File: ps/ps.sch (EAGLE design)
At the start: 73 parts, among them IC1 LM675, J1 NE-2, Q1 NPN-D, Q2 NPN-D, U2 LM317, U3 TLC555CD, U4 LM317, U5 LM317

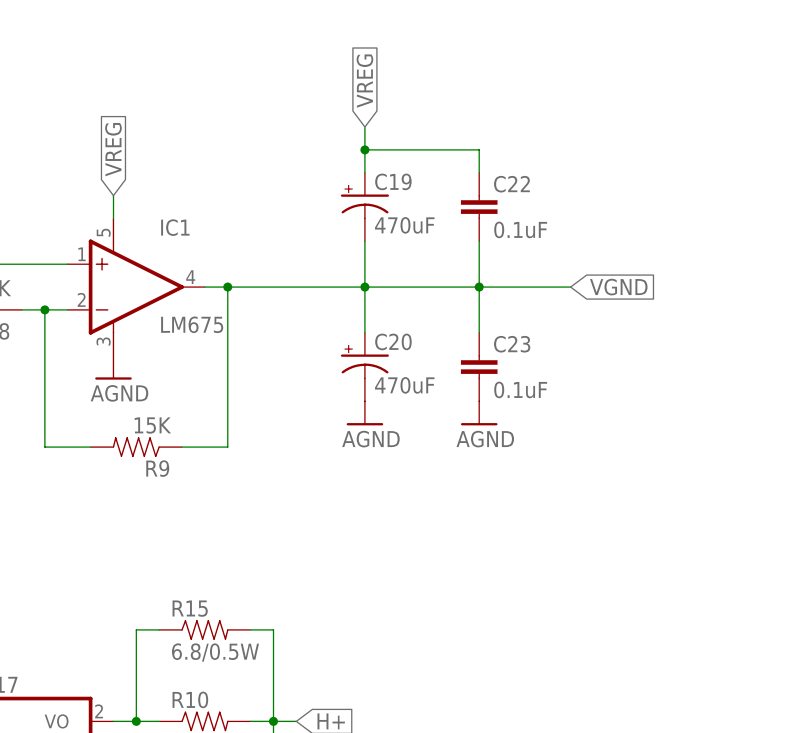
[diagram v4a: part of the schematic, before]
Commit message: Unneeded caps removed
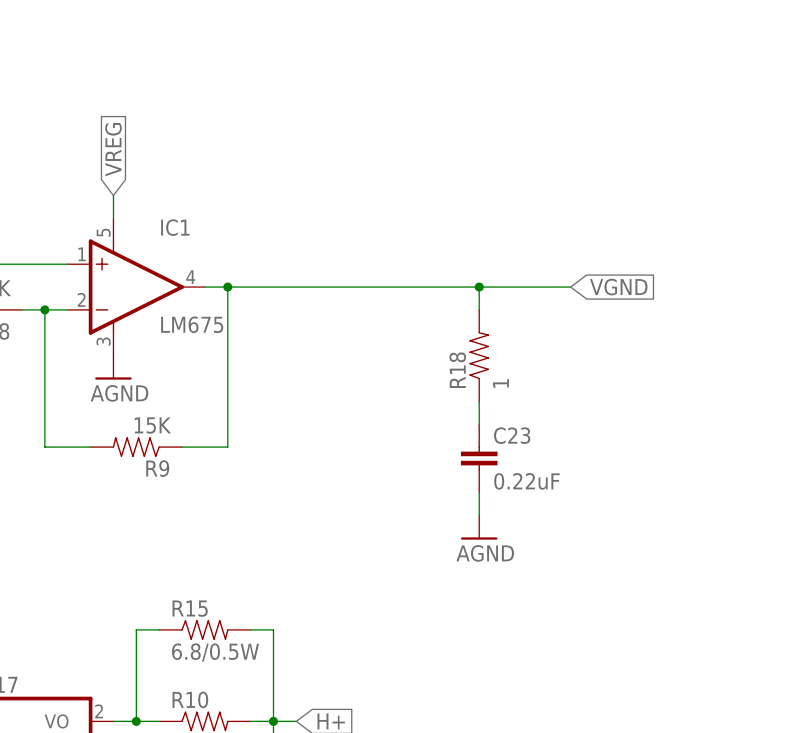
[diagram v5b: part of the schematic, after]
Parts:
- removed C19, C20: 470uF, SparkFun-Capacitors:CAP_POLPTH4
- removed C22: 0.1uF, SparkFun-Capacitors:0.1UF-25V-5%(0603)
- added R18: 1, SparkFun-Resistors:RESISTORPTH-1/4W
- C23: value 0.1uF -> 0.22uF; device SparkFun-Capacitors:0.1UF-25V-5%(0603) -> SparkFun-Capacitors:0.22UF-25V-10%(0603)
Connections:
- new net N$17: C23.1, R18.1
- net AGND: no longer C20.-
- net VGND: now also R18.2; no longer C19.-, C20.+, C22.2, C23.1
- net VREG: no longer C19.+, C22.1
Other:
- moved on the sheet: C23
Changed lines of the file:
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@@
 <part name="C2" library="SparkFun-Capacitors" deviceset="CAP_POL" device="PTH4" value="470uF"/>
 <part name="SUPPLY1" library="SparkFun-Aesthetics" deviceset="VCC" device=""/>
-<part name="C20" library="SparkFun-Capacitors" deviceset="CAP_POL" device="PTH4" value="470uF"/>
-<part name="C19" library="SparkFun-Capacitors" deviceset="CAP_POL" device="PTH4" value="470uF"/>
-<part name="C22" library="SparkFun-Capacitors" deviceset="0.1UF-25V-5%(0603)" device="" value="0.1uF"/>
-<part name="C23" library="SparkFun-Capacitors" deviceset="0.1UF-25V-5%(0603)" device="" value="0.1uF"/>
+<part name="C23" library="SparkFun-Capacitors" deviceset="0.22UF-25V-10%(0603)" device="" value="0.22uF"/>
 <part name="LOGO1" library="my" deviceset="LOGO-MANTIS" device=""/>
 <part name="X1" library="con-wago-508" deviceset="W237-02P" device=""/>
@@
 <part name="U$1" library="SparkFun-Aesthetics" deviceset="AGND" device=""/>
 <part name="U$2" library="SparkFun-Aesthetics" deviceset="AGND" device=""/>
-<part name="U$3" library="SparkFun-Aesthetics" deviceset="AGND" device=""/>
 <part name="U$4" library="SparkFun-Aesthetics" deviceset="AGND" device=""/>
 <part name="U$5" library="SparkFun-Aesthetics" deviceset="AGND" device=""/>
@@
 <part name="R16" library="SparkFun-Resistors" deviceset="RESISTOR" device="PTH-1/4W" value="0.33"/>
 <part name="R17" library="SparkFun-Resistors" deviceset="RESISTOR" device="PTH-1/4W-VERT" value="1"/>
+<part name="R18" library="SparkFun-Resistors" deviceset="RESISTOR" device="PTH-1/4W" value="1"/>
 </parts>
 <sheets>
@@
 <instance part="C2" gate="G$1" x="15.24" y="154.94"/>
 <instance part="SUPPLY1" gate="G$1" x="12.7" y="172.72" rot="R90"/>
-<instance part="C20" gate="G$1" x="266.7" y="200.66"/>
-<instance part="C19" gate="G$1" x="266.7" y="218.44"/>
-<instance part="C22" gate="G$1" x="279.4" y="215.9"/>
-<instance part="C23" gate="G$1" x="279.4" y="198.12"/>
+<instance part="C23" gate="G$1" x="279.4" y="187.96"/>
 <instance part="LOGO1" gate="G$1" x="175.26" y="43.18"/>
 <instance part="X1" gate="-1" x="25.4" y="213.36"/>
@@
 <instance part="U$1" gate="G$1" x="15.24" y="132.08"/>
 <instance part="U$2" gate="G$1" x="215.9" y="190.5"/>
-<instance part="U$3" gate="G$1" x="266.7" y="193.04"/>
-<instance part="U$4" gate="G$1" x="279.4" y="193.04"/>
+<instance part="U$4" gate="G$1" x="279.4" y="180.34"/>
 <instance part="U$5" gate="G$1" x="33.02" y="208.28" rot="R90"/>
 <instance part="U$6" gate="G$1" x="68.58" y="208.28" rot="R90"/>
@@
 <instance part="R16" gate="G$1" x="25.4" y="172.72"/>
 <instance part="R17" gate="G$1" x="269.24" y="144.78"/>
+<instance part="R18" gate="G$1" x="279.4" y="200.66" rot="R90"/>
 </instances>
 <busses>
@@
 <pinref part="IC1" gate="G$1" pin="OUT"/>
 <wire x1="251.46" y1="208.28" x2="248.92" y2="208.28" width="0.1524" layer="91"/>
-<wire x1="251.46" y1="208.28" x2="266.7" y2="208.28" width="0.1524" layer="91"/>
+<wire x1="251.46" y1="208.28" x2="279.4" y2="208.28" width="0.1524" layer="91"/>
 <junction x="251.46" y="208.28"/>
 <label x="289.56" y="208.28" size="1.778" layer="95" xref="yes"/>
-<pinref part="C20" gate="G$1" pin="+"/>
-<wire x1="266.7" y1="208.28" x2="279.4" y2="208.28" width="0.1524" layer="91"/>
 <wire x1="279.4" y1="208.28" x2="289.56" y2="208.28" width="0.1524" layer="91"/>
-<wire x1="266.7" y1="203.2" x2="266.7" y2="208.28" width="0.1524" layer="91"/>
-<junction x="266.7" y="208.28"/>
-<pinref part="C19" gate="G$1" pin="-"/>
-<wire x1="266.7" y1="208.28" x2="266.7" y2="213.36" width="0.1524" layer="91"/>
-<pinref part="C22" gate="G$1" pin="2"/>
-<wire x1="279.4" y1="208.28" x2="279.4" y2="213.36" width="0.1524" layer="91"/>
 <junction x="279.4" y="208.28"/>
-<pinref part="C23" gate="G$1" pin="1"/>
-<wire x1="279.4" y1="208.28" x2="279.4" y2="203.2" width="0.1524" layer="91"/>
+<wire x1="279.4" y1="208.28" x2="279.4" y2="205.74" width="0.1524" layer="91"/>
+<pinref part="R18" gate="G$1" pin="2"/>
 </segment>
 <segment>
@@
 <wire x1="238.76" y1="215.9" x2="238.76" y2="218.44" width="0.1524" layer="91"/>
 <label x="238.76" y="218.44" size="1.778" layer="95" rot="R90" xref="yes"/>
-</segment>
-<segment>
-<pinref part="C22" gate="G$1" pin="1"/>
-<wire x1="279.4" y1="220.98" x2="279.4" y2="223.52" width="0.1524" layer="91"/>
-<pinref part="C19" gate="G$1" pin="+"/>
-<wire x1="279.4" y1="223.52" x2="266.7" y2="223.52" width="0.1524" layer="91"/>
-<wire x1="266.7" y1="223.52" x2="266.7" y2="220.98" width="0.1524" layer="91"/>
-<wire x1="266.7" y1="223.52" x2="266.7" y2="226.06" width="0.1524" layer="91"/>
-<junction x="266.7" y="223.52"/>
-<label x="266.7" y="226.06" size="1.778" layer="95" rot="R90" xref="yes"/>
 </segment>
 <segment>
@@
 </segment>
 <segment>
-<pinref part="C20" gate="G$1" pin="-"/>
-<pinref part="U$3" gate="G$1" pin="AGND"/>
-</segment>
-<segment>
 <pinref part="C23" gate="G$1" pin="2"/>
 <pinref part="U$4" gate="G$1" pin="AGND"/>
+<wire x1="279.4" y1="182.88" x2="279.4" y2="185.42" width="0.1524" layer="91"/>
 </segment>
 <segment>
@@
 </segment>
 </net>
+<net name="N$17" class="1">
+<segment>
+<pinref part="C23" gate="G$1" pin="1"/>
+<pinref part="R18" gate="G$1" pin="1"/>
+<wire x1="279.4" y1="195.58" x2="279.4" y2="193.04" width="0.1524" layer="91"/>
+</segment>
+</net>
